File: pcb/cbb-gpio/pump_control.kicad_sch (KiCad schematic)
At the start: 6 parts, among them Q5 AO3400A

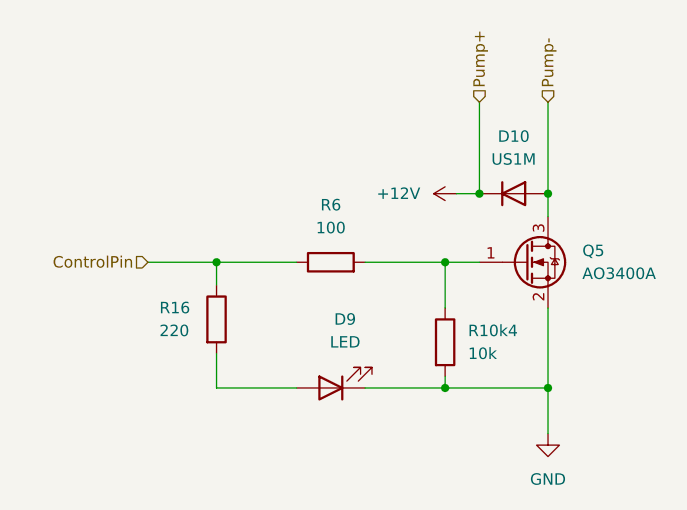
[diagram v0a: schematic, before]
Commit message: reduce brightness of channel indicator led
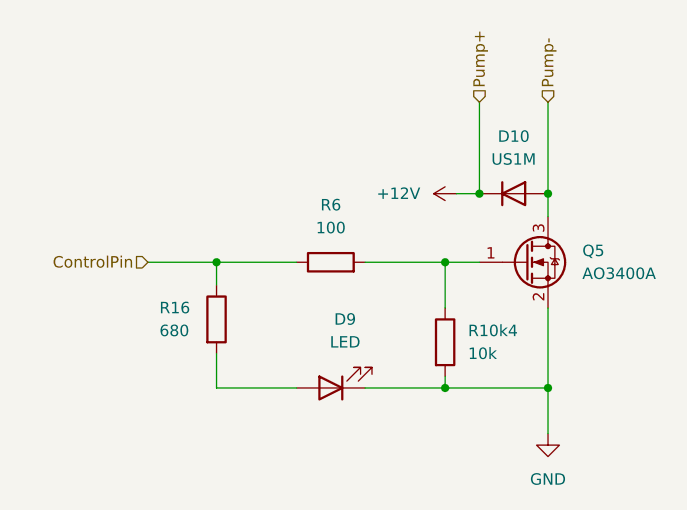
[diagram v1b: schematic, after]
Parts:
- R16: value 220 -> 680; MPN C22962 -> C23228
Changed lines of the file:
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@@
 			)
 		)
-		(property "Value" "220"
+		(property "Value" "680"
 			(at 92.71 90.17 0)
 			(effects
@@
 			)
 		)
-		(property "MPN" "C22962"
+		(property "MPN" "C23228"
 			(at 99.06 88.9 90)
 			(effects
@@
 		)
 		(instances
+			(project ""
+				(path "/08e8e2b9-5c8d-4651-bb52-679dee8728f5"
+					(reference "R16")
+					(unit 1)
+				)
+			)
 			(project ""
 				(path "/5575e3e9-07ff-42ca-b261-f5e11b540bc9/3509e54a-7fe2-4c9a-a501-131594e610ec"
@@
 		)
 	)
+	(sheet_instances
+		(path "/"
+			(page "1")
+		)
+	)
